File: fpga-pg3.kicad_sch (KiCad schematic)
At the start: 2 parts, among them U6 XC7A15T-CSG325

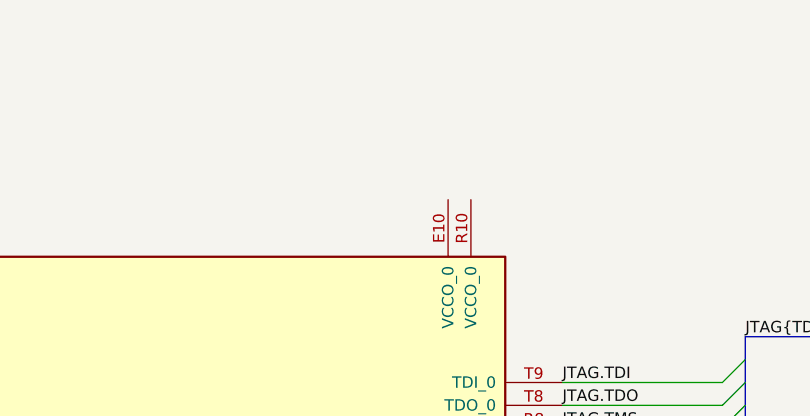
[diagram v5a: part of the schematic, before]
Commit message: placed decoupling caps for fpga
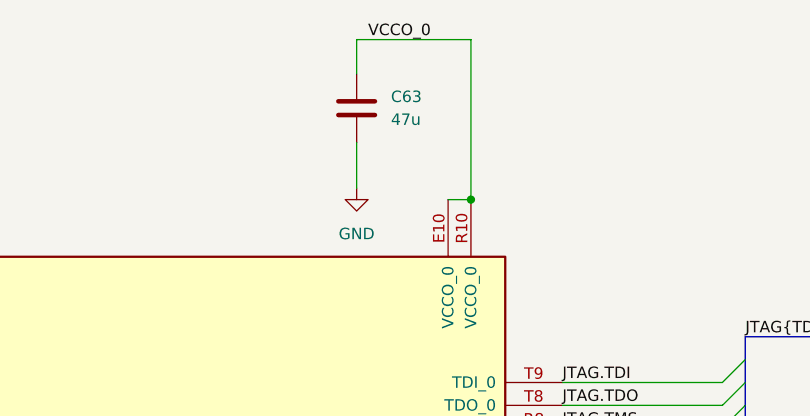
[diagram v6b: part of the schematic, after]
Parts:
- added C63: 47u, Capacitor_SMD:C_1210_3225Metric, symbol Device:C
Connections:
- net VCCO_0: now reaches U6.E10 (VCCO_0)
- net VCCO_0: now also U6.R10 (VCCO_0), C63.1
- new net GND: C63.2
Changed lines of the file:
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@@
 	(generator_version "9.0")
 	(paper "A3")
+	(junction
+		(at 245.11 46.99)
+		(diameter 0)
+		(color 0 0 0 0)
+	)
 	(bus_entry
 		(at 275.59 69.85)
@@
 		)
 	)
+	(wire
+		(pts
+			(xy 232.41 40.64) (xy 232.41 45.72)
+		)
+		(stroke
+			(width 0)
+			(type default)
+		)
+	)
 	(bus
 		(pts
@@
 		)
 	)
+	(wire
+		(pts
+			(xy 245.11 29.21) (xy 245.11 46.99)
+		)
+		(stroke
+			(width 0)
+			(type default)
+		)
+	)
 	(bus
 		(pts
@@
 	(wire
 		(pts
+			(xy 242.57 46.99) (xy 245.11 46.99)
+		)
+		(stroke
+			(width 0)
+			(type default)
+		)
+	)
+	(wire
+		(pts
 			(xy 144.78 149.86) (xy 179.07 149.86)
 		)
@@
 	(wire
 		(pts
+			(xy 232.41 29.21) (xy 232.41 33.02)
+		)
+		(stroke
+			(width 0)
+			(type default)
+		)
+	)
+	(wire
+		(pts
 			(xy 144.78 172.72) (xy 179.07 172.72)
 		)
@@
 		(pts
 			(xy 275.59 64.77) (xy 275.59 62.23)
+		)
+		(stroke
+			(width 0)
+			(type default)
+		)
+	)
+	(wire
+		(pts
+			(xy 232.41 29.21) (xy 245.11 29.21)
 		)
 		(stroke
@@
 	(label "JTAG{TDI TDO TMS TCK}"
 		(at 275.59 62.23 0)
+		(effects
+			(font
+				(size 1.27 1.27)
+			)
+			(justify left bottom)
+		)
+	)
+	(label "VCCO_0"
+		(at 233.68 29.21 0)
 		(effects
 			(font
@@
 			)
 			(justify left)
+		)
+	)
+	(symbol
+		(lib_id "Device:C")
+		(at 232.41 36.83 0)
+		(unit 1)
+		(exclude_from_sim no)
+		(in_bom yes)
+		(on_board yes)
+		(dnp no)
+		(fields_autoplaced yes)
+		(property "Reference" "C63"
+			(at 236.22 35.5599 0)
+			(effects
+				(font
+					(size 1.27 1.27)
+				)
+				(justify left)
+			)
+		)
+		(property "Value" "47u"
+			(at 236.22 38.0999 0)
+			(effects
+				(font
+					(size 1.27 1.27)
+				)
+				(justify left)
+			)
+		)
+		(property "Footprint" "Capacitor_SMD:C_1210_3225Metric"
+			(at 233.3752 40.64 0)
+			(effects
+				(font
+					(size 1.27 1.27)
+				)
+				(hide yes)
+			)
+		)
+		(property "Datasheet" "~"
+			(at 232.41 36.83 0)
+			(effects
+				(font
+					(size 1.27 1.27)
+				)
+				(hide yes)
+			)
+		)
+		(property "Description" "Unpolarized capacitor"
+			(at 232.41 36.83 0)
+			(effects
+				(font
+					(size 1.27 1.27)
+				)
+				(hide yes)
+			)
+		)
+		(pin "2"
+		)
+		(pin "1"
+		)
+		(instances
+			(project "logix-core"
+				(path "/cf3b7c5f-6ddc-4e3f-9529-0bcf5eec6f23/824409ff-e0aa-4944-ad80-228eadb659f9/9208eeea-aa23-4f0a-a0f4-52abaf751fbe"
+					(reference "C63")
+					(unit 1)
+				)
+			)
 		)
 	)
@@
 				)
 			)
+		)
+	)
+	(symbol
+		(lib_id "power:GND")
+		(at 232.41 45.72 0)
+		(unit 1)
+		(exclude_from_sim no)
+		(in_bom yes)
+		(on_board yes)
+		(dnp no)
+		(fields_autoplaced yes)
+		(property "Reference" "#PWR067"
+			(at 232.41 52.07 0)
+			(effects
+				(font
+					(size 1.27 1.27)
+				)
+				(hide yes)
+			)
+		)
+		(property "Value" "GND"
+			(at 232.41 50.8 0)
+			(effects
+				(font
+					(size 1.27 1.27)
+				)
+			)
+		)
+		(property "Footprint" ""
+			(at 232.41 45.72 0)
+			(effects
+				(font
+					(size 1.27 1.27)
+				)
+				(hide yes)
+			)
+		)
+		(property "Datasheet" ""
+			(at 232.41 45.72 0)
+			(effects
+				(font
+					(size 1.27 1.27)
+				)
+				(hide yes)
+			)
+		)
+		(property "Description" "Power symbol creates a global label with name \"GND\" , ground"
+			(at 232.41 45.72 0)
+			(effects
+				(font
+					(size 1.27 1.27)
+				)
+				(hide yes)
+			)
+		)
+		(pin "1"
+		)
+		(instances
+			(project "logix-core"
+				(path "/cf3b7c5f-6ddc-4e3f-9529-0bcf5eec6f23/824409ff-e0aa-4944-ad80-228eadb659f9/9208eeea-aa23-4f0a-a0f4-52abaf751fbe"
+					(reference "#PWR067")
+					(unit 1)
+				)
+			)

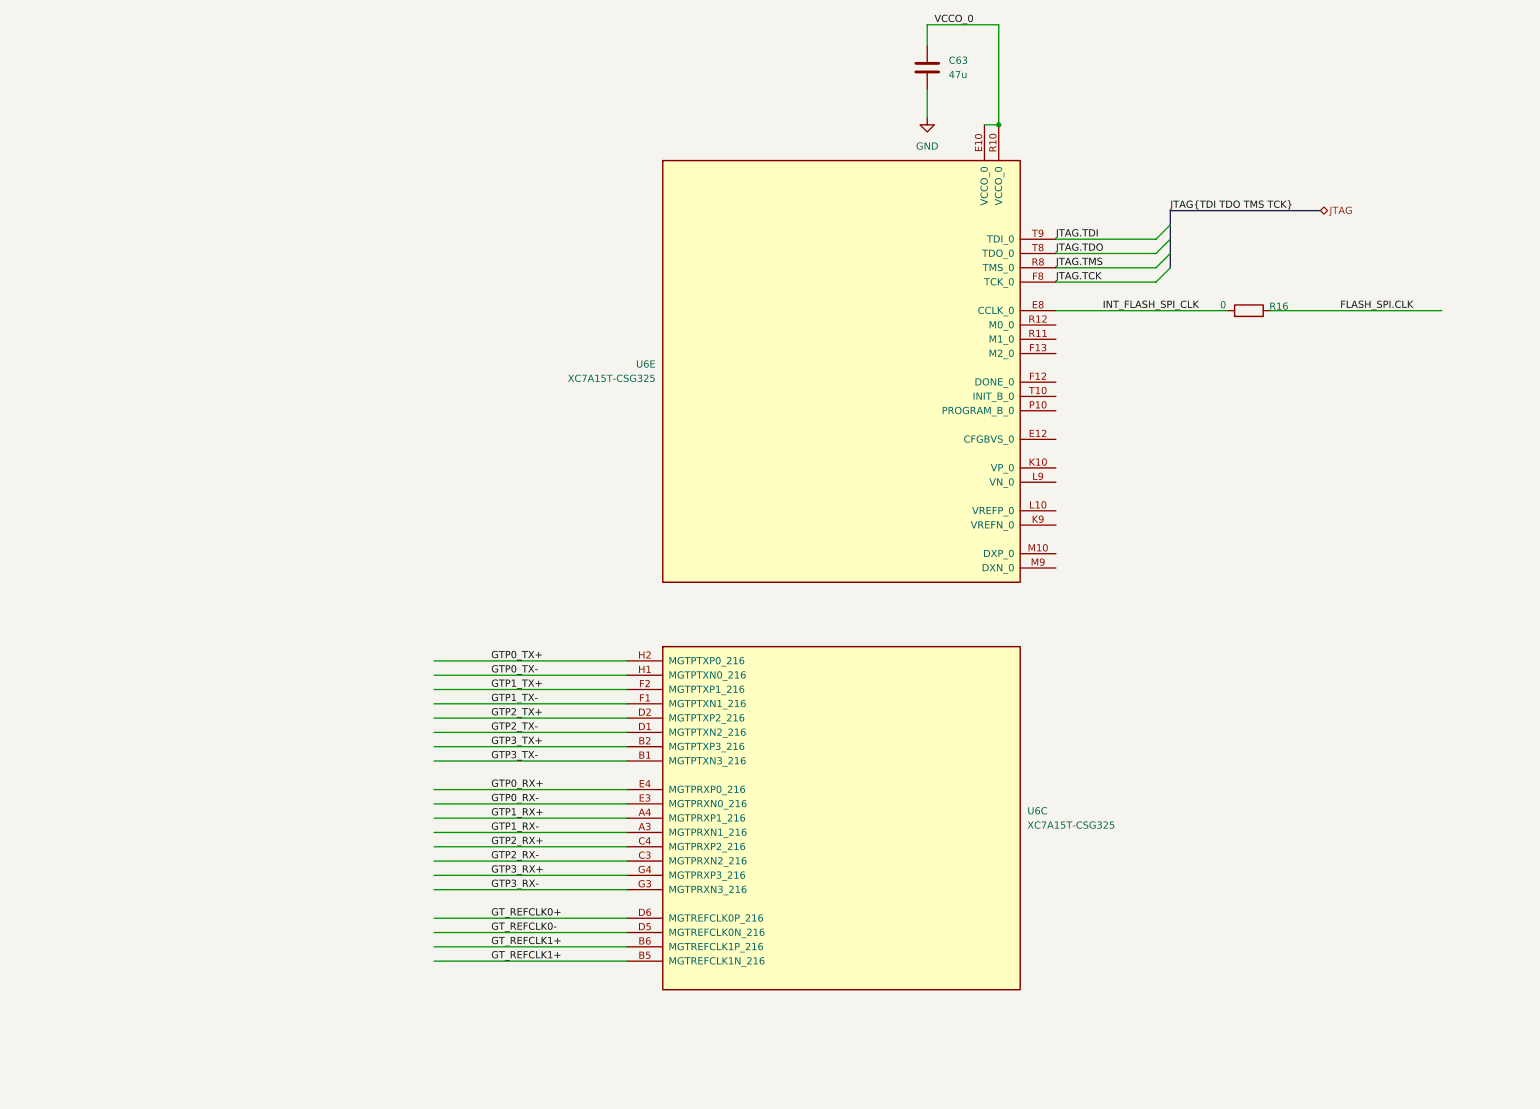
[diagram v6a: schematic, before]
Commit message: started changing package, added correct decoupling
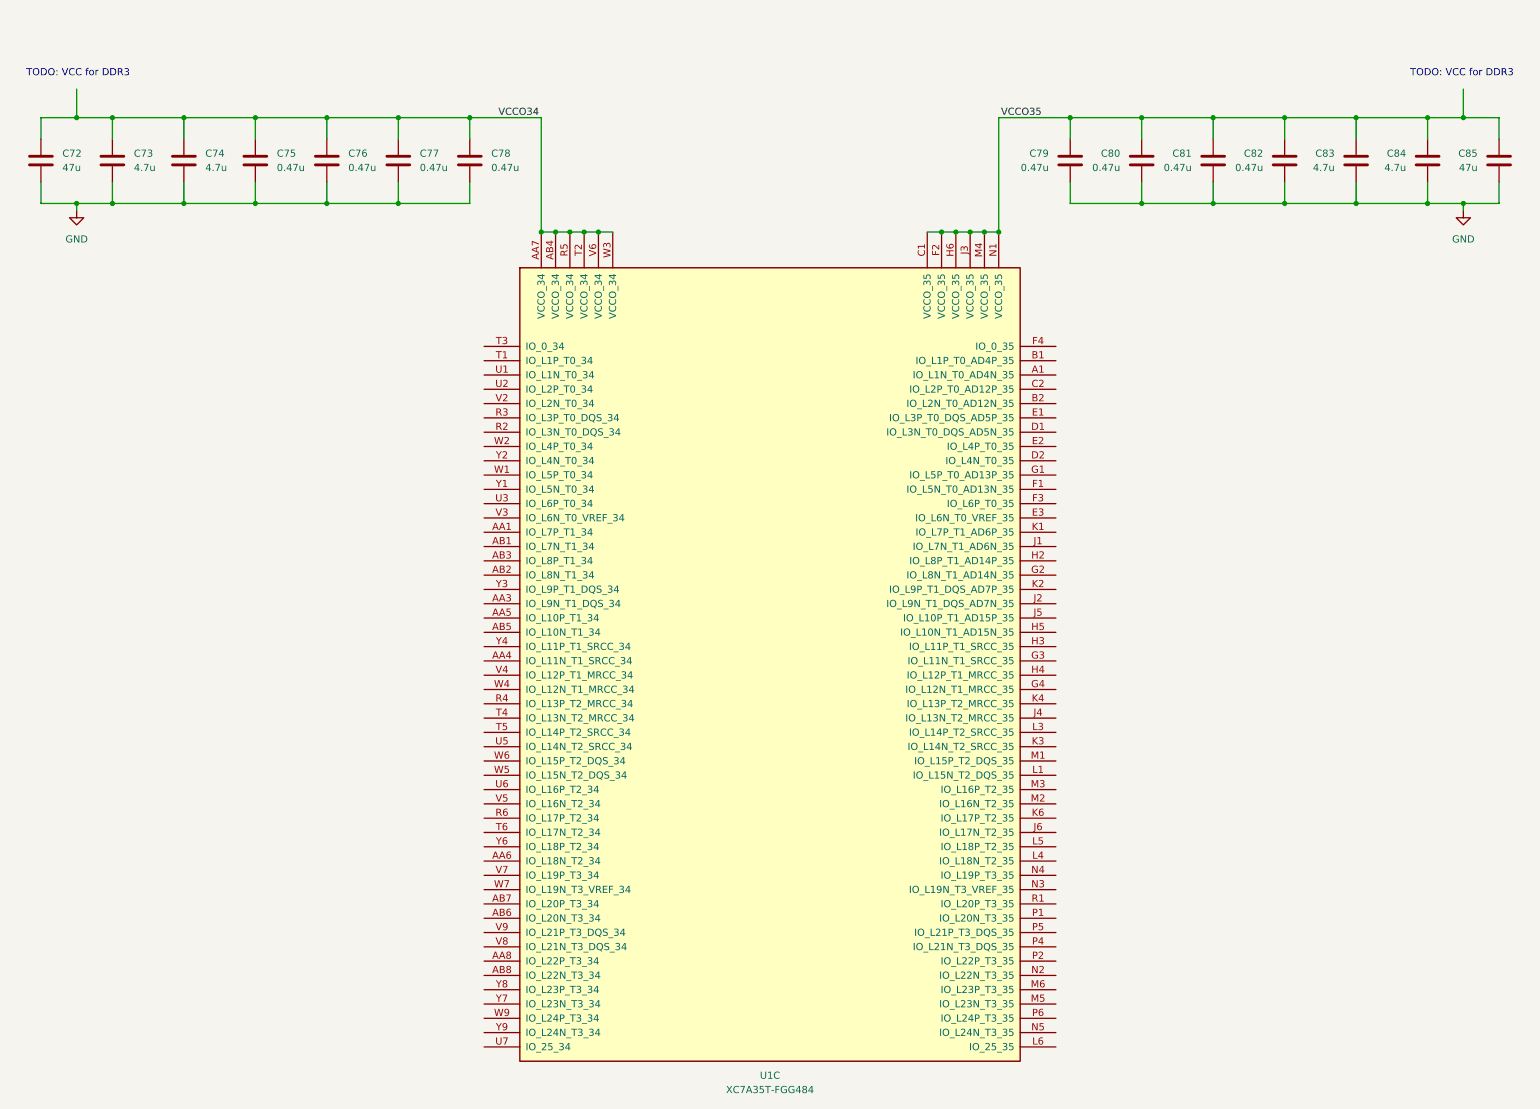
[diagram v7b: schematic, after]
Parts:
- removed C63: 47u, Capacitor_SMD:C_1210_3225Metric, symbol Device:C
- removed R16: 0, Resistor_SMD:R_0402_1005Metric_Pad0.72x0.64mm_HandSolder, symbol Device:R
- removed U6: XC7A15T-CSG325, Package_BGA:Xilinx_CSG325, symbol FPGA_Xilinx_Artix7:XC7A15T-CSG325
- added C72, C85: 47u, Capacitor_SMD:C_1210_3225Metric, symbol Device:C
- added C73, C74, C83, C84: 4.7u, Capacitor_SMD:C_0402_1005Metric, symbol Device:C
- added C75, C76, C77, C78, C79, C80, C81, C82: 0.47u, Capacitor_SMD:C_0402_1005Metric, symbol Device:C
- added U1: XC7A35T-FGG484, Package_BGA:Xilinx_FGG484, symbol FPGA_Xilinx_Artix7:XC7A35T-FGG484
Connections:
- net GND: now also C72.2, C73.2, C74.2, C75.2, C76.2, C77.2, C78.2, C79.2, C80.2, C81.2, C82.2, C83.2, C84.2, C85.2
- new net VCCO34: C72.1, C73.1, C74.1, C75.1, C76.1, C77.1, C78.1, U1.AA7 (VCCO_34), U1.AB4 (VCCO_34), U1.R5 (VCCO_34), U1.T2 (VCCO_34), U1.V6 (VCCO_34), U1.W3 (VCCO_34)
- new net VCCO35: C79.1, C80.1, C81.1, C82.1, C83.1, C84.1, C85.1, U1.C1 (VCCO_35), U1.F2 (VCCO_35), U1.H6 (VCCO_35), U1.J3 (VCCO_35), U1.M4 (VCCO_35), U1.N1 (VCCO_35)
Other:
- note added: "TODO: VCC for DDR3"

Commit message: connected almost all ddr3 pins, started placing decoupling caps
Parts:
- added R11, R12, R13, R14, R15: 0, Resistor_SMD:R_0402_1005Metric_Pad0.72x0.64mm_HandSolder, symbol Device:R
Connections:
- net DDR3_ADDR13: now reaches U1.A1 (IO_L1N_T0_AD4N_35)
- net DDR3_ADDR14: now reaches U1.B1 (IO_L1P_T0_AD4P_35)
- net DDR3_ADDR11: now reaches U1.B2 (IO_L2N_T0_AD12N_35)
- net DDR3_ADDR12: now reaches U1.C2 (IO_L2P_T0_AD12P_35)
- net DDR3_CLK-: now reaches U1.D1 (IO_L3N_T0_DQS_AD5N_35)
- net DDR3_ADDR9: now reaches U1.D2 (IO_L4N_T0_35)
- net DDR3_CLK+: now reaches U1.E1 (IO_L3P_T0_DQS_AD5P_35)
- net DDR3_ADDR10: now reaches U1.E2 (IO_L4P_T0_35)
- net DDR3_ADDR7: now reaches U1.F1 (IO_L5N_T0_AD13N_35)
- net DDR3_ADDR6: now reaches U1.F3 (IO_L6P_T0_35)
- net DDR3_ADDR8: now reaches U1.G1 (IO_L5P_T0_AD13P_35)
- net DDR3_ADDR2: now reaches U1.G2 (IO_L8N_T1_AD14N_35)
- net DDR3_ADDR3: now reaches U1.H2 (IO_L8P_T1_AD14P_35)
- net DDR3_BLOCK_ADDR0: now reaches U1.H3 (IO_L11P_T1_SRCC_35)
- net DDR3_BLOCK_ADDR1: now reaches U1.H5 (IO_L10N_T1_AD15N_35)
- net DDR3_ADDR4: now reaches U1.J1 (IO_L7N_T1_AD6N_35)
- net DDR3_ADDR0: now reaches U1.J2 (IO_L9N_T1_DQS_AD7N_35)
- net DDR3_BLOCK_ADDR2: now reaches U1.J5 (IO_L10P_T1_AD15P_35)
- net DDR3_ADDR5: now reaches U1.K1 (IO_L7P_T1_AD6P_35)
- net DDR3_ADDR1: now reaches U1.K2 (IO_L9P_T1_DQS_AD7P_35)
- net DDR3_CLK_EN: now reaches U1.L1 (IO_L15N_T2_DQS_35)
- net DDR3_CS#: now reaches U1.M1 (IO_L15P_T2_DQS_35)
- net DDR3_ODT: now reaches U1.M3 (IO_L16P_T2_35)
- net DDR3_DQ5: now reaches U1.M5 (IO_L23N_T3_35)
- net DDR3_DQ4: now reaches U1.M6 (IO_L23P_T3_35)
- net DDR3_DQ3: now reaches U1.N2 (IO_L22N_T3_35)
- net DDR3_LDM: now reaches U1.N4 (IO_L19P_T3_35)
- net DDR3_DQ7: now reaches U1.N5 (IO_L24N_T3_35)
- net DDR3_DQ1: now reaches U1.P1 (IO_L20N_T3_35)
- net DDR3_DQ2: now reaches U1.P2 (IO_L22P_T3_35)
- net DDR3_LDQS-: now reaches U1.P4 (IO_L21N_T3_DQS_35)
- net DDR3_LDQS+: now reaches U1.P5 (IO_L21P_T3_DQS_35)
- net DDR3_DQ6: now reaches U1.P6 (IO_L24P_T3_35)
- net DDR3_DQ0: now reaches U1.R1 (IO_L20P_T3_35)
- net DDR3_UDQS-: now reaches U1.R2 (IO_L3N_T0_DQS_34)
- net DDR3_UDQS+: now reaches U1.R3 (IO_L3P_T0_DQS_34)
- net DDR3_UDM: now reaches U1.T1 (IO_L1P_T0_34)
- net DDR3_DQ8: now reaches U1.U1 (IO_L1N_T0_34)
- net DDR3_DQ9: now reaches U1.U2 (IO_L2P_T0_34)
- net DDR3_DQ15: now reaches U1.U3 (IO_L6P_T0_34)
- net DDR3_DQ10: now reaches U1.V2 (IO_L2N_T0_34)
- net DDR3_DQ13: now reaches U1.W1 (IO_L5P_T0_34)
- net DDR3_DQ11: now reaches U1.W2 (IO_L4P_T0_34)
- net DDR3_DQ14: now reaches U1.Y1 (IO_L5N_T0_34)
- net DDR3_DQ12: now reaches U1.Y2 (IO_L4N_T0_34)
- new net FLASH_SPI.CS#: R15.1
- new net FLASH_SPI.D0: R11.1
- new net FLASH_SPI.D1: R12.1
- new net FLASH_SPI.D2: R13.1
- new net FLASH_SPI.D3: R14.1
- new net INT_FLASH_SPI_CS#: R15.2
- new net INT_FLASH_SPI_D0: R11.2
- new net INT_FLASH_SPI_D1: R12.2
- new net INT_FLASH_SPI_D2: R13.2
- new net INT_FLASH_SPI_D3: R14.2
